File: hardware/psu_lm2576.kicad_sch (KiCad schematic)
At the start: 5 parts, among them U11 LM2576S-5_0_TR, U13 100uH

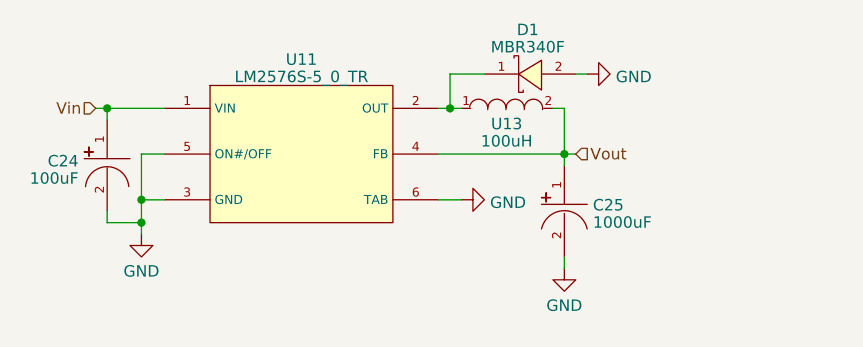
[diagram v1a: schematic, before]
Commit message: start working on mainboard pcb layout
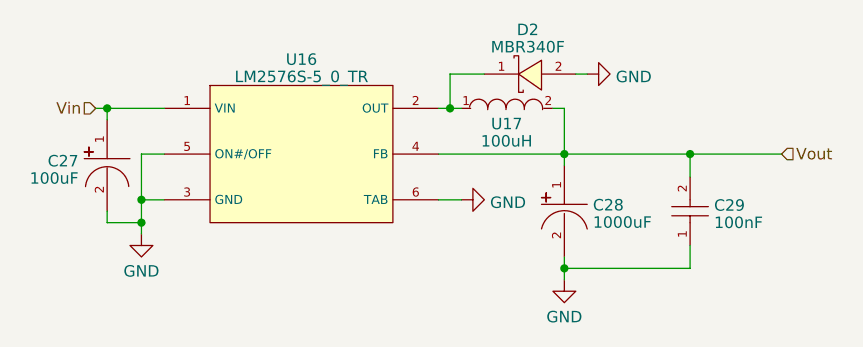
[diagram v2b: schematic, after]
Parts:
- added C29: 100nF, jlc_footprints:C0402, symbol jlc:CC0402KRX7R8BB104
- renumbered C24 to C27, C25 to C28, D1 to D2, U11 to U16, U13 to U17
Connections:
- net GND: now also C29.1
- net Vout: now also C29.2
